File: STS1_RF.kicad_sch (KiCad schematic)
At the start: 79 parts, among them J1 UHF, Q1 SQ2318, Q3 SQ2318, Q4 SQ2318, U10 TQP3M9036, U11 NL17SV04XV5T2G, U16 F2972, U2 LP2985-1.8, U4 74LVC2G74, U5 TYKTBCSANF-26.000000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

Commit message: Fix mismatch between footprint and part number for C48, C72, C74, R13, R24, R21, R27, R28, R30, R31
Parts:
- R13, R21, R24: PartNumber CR0402-FX-3302GLF -> (none)
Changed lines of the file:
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@@
       (effects (font (size 1.27 1.27)) hide)
     )
-    (property "Description" "Resistor, 0402, 5%, 1/16W" (id 4) (at 157.48 166.37 0)
+    (property "Description" "" (id 4) (at 157.48 166.37 0)
       (effects (font (size 1.27 1.27)) hide)
     )
@@
       (effects (font (size 1.27 1.27)) hide)
     )
-    (property "PartNumber" "CR0402-FX-3302GLF" (id 6) (at 157.48 166.37 0)
+    (property "PartNumber" "" (id 6) (at 157.48 166.37 0)
       (effects (font (size 1.27 1.27)) hide)
     )
@@
       (effects (font (size 1.27 1.27)) hide)
     )
-    (property "Description" "Resistor, 0402, 5%, 1/16W" (id 4) (at 60.96 121.92 0)
+    (property "Description" "" (id 4) (at 60.96 121.92 0)
       (effects (font (size 1.27 1.27)) hide)
     )
@@
       (effects (font (size 1.27 1.27)) hide)
     )
-    (property "PartNumber" "CR0402-FX-3302GLF" (id 6) (at 60.96 121.92 0)
+    (property "PartNumber" "" (id 6) (at 60.96 121.92 0)
       (effects (font (size 1.27 1.27)) hide)
     )
@@
       (effects (font (size 1.27 1.27)) hide)
     )
-    (property "Description" "Resistor, 0402, 5%, 1/16W" (id 4) (at 72.39 121.92 0)
+    (property "Description" "" (id 4) (at 72.39 121.92 0)
       (effects (font (size 1.27 1.27)) hide)
     )
@@
       (effects (font (size 1.27 1.27)) hide)
     )
-    (property "PartNumber" "CR0402-FX-3302GLF" (id 6) (at 72.39 121.92 0)
-      (effects (font (size 1.27 1.27)) hide)
-    )
+    (property "PartNumber" "" (id 6) (at 72.39 121.92 0)
+      (effects (font (size 1.27 1.27)) hide)
+    )

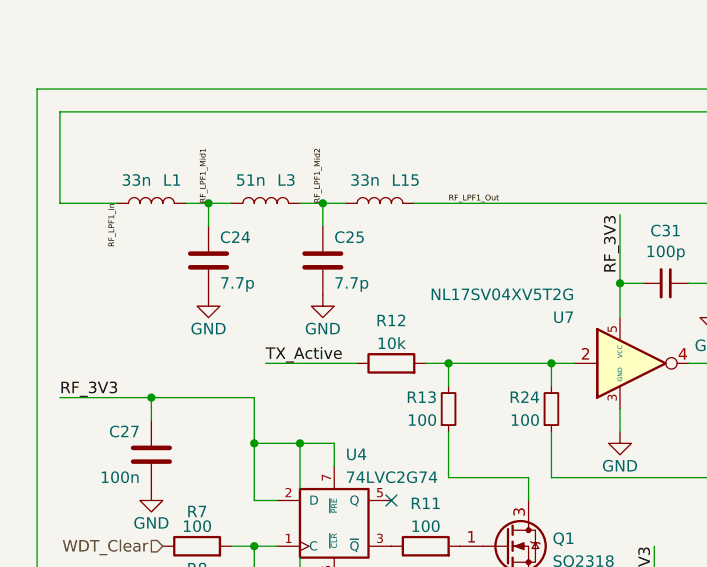
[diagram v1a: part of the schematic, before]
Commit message: Update values of components in the RF subsystem and swap CL instead of LC filter (L14 and C67)
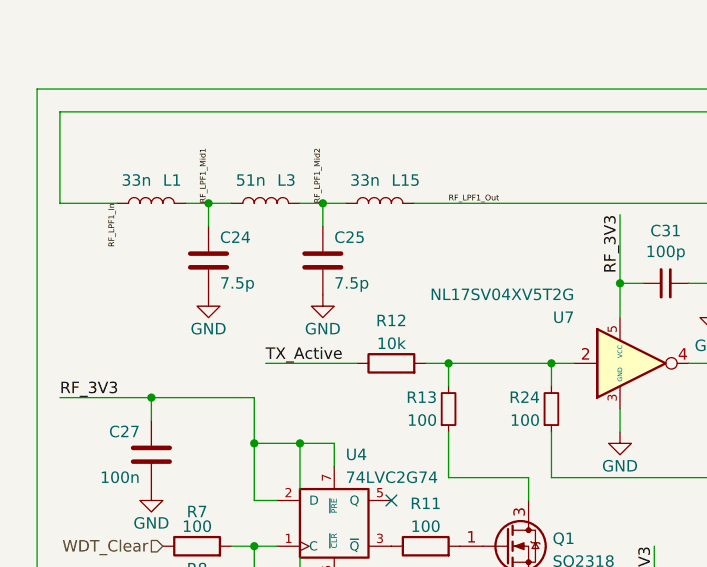
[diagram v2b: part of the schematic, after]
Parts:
- C24, C25: value 7.7p -> 7.5p
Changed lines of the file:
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@@
       (effects (font (size 1.27 1.27)) (justify left))
     )
-    (property "Value" "7.7p" (id 1) (at 48.26 107.95 0)
+    (property "Value" "7.5p" (id 1) (at 48.26 107.95 0)
       (effects (font (size 1.27 1.27)) (justify left))
     )
@@
       (effects (font (size 1.27 1.27)) (justify left))
     )
-    (property "Value" "7.7p" (id 1) (at 35.56 107.95 0)
-      (effects (font (size 1.27 1.27)) (justify left))
-    )
+    (property "Value" "7.5p" (id 1) (at 35.56 107.95 0)
+      (effects (font (size 1.27 1.27)) (justify left))
+    )

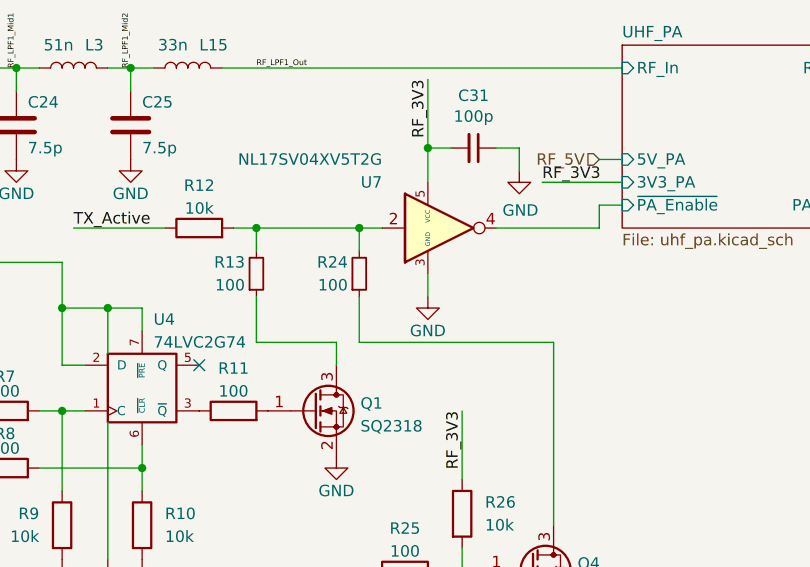
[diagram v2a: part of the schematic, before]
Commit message: Add latchup protection circuits
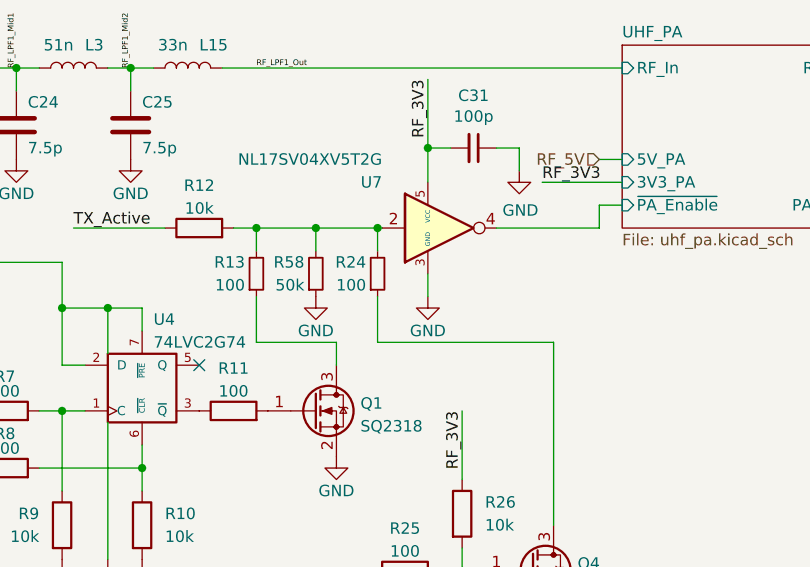
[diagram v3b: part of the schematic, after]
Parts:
- added R58: 50k, Resistor_SMD:R_0603_1608Metric, symbol Device:R_Small
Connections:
- net GND: now also R58.1
- net at R12.2, R13.2, R24.2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: now also R58.2
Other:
- moved on the sheet: R24
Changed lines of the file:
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@@
   (junction (at 158.75 73.66) (diameter 0) (color 0 0 0 0)
   )
+  (junction (at 74.422 116.84) (diameter 0) (color 0 0 0 0)
+  )
   (junction (at 66.04 66.04) (diameter 0) (color 0 0 0 0)
   )
@@
   (junction (at 181.61 147.32) (diameter 0) (color 0 0 0 0)
   )
-  (junction (at 72.39 116.84) (diameter 0) (color 0 0 0 0)
-  )
   (junction (at 248.92 101.6) (diameter 0) (color 0 0 0 0)
   )
@@
   )
   (junction (at 152.4 50.8) (diameter 0) (color 0 0 0 0)
+  )
+  (junction (at 67.564 116.84) (diameter 0) (color 0 0 0 0)
   )
   (junction (at 48.26 143.51) (diameter 0) (color 0 0 0 0)
@@
     (stroke (width 0) (type default) (color 0 0 0 0))
   )
+  (wire (pts (xy 67.564 116.84) (xy 74.422 116.84))
+    (stroke (width 0) (type default) (color 0 0 0 0))
+  )
   (wire (pts (xy 100.33 55.88) (xy 120.65 55.88))
     (stroke (width 0) (type default) (color 0 0 0 0))
@@
     (stroke (width 0) (type default) (color 0 0 0 0))
   )
-  (wire (pts (xy 72.39 129.54) (xy 93.98 129.54))
-    (stroke (width 0) (type default) (color 0 0 0 0))
-  )
   (wire (pts (xy 48.26 55.88) (xy 48.26 66.04))
     (stroke (width 0) (type default) (color 0 0 0 0))
@@
     (stroke (width 0) (type default) (color 0 0 0 0))
   )
+  (wire (pts (xy 93.98 129.54) (xy 74.422 129.54))
+    (stroke (width 0) (type default) (color 0 0 0 0))
+  )
   (wire (pts (xy 149.86 153.67) (xy 152.4 153.67))
     (stroke (width 0) (type default) (color 0 0 0 0))
@@
     (stroke (width 0) (type default) (color 0 0 0 0))
   )
-  (wire (pts (xy 72.39 124.46) (xy 72.39 129.54))
-    (stroke (width 0) (type default) (color 0 0 0 0))
-  )
   (wire (pts (xy 152.4 99.06) (xy 170.18 99.06))
     (stroke (width 0) (type default) (color 0 0 0 0))
@@
     (stroke (width 0) (type default) (color 0 0 0 0))
   )
+  (wire (pts (xy 74.422 129.54) (xy 74.422 124.46))
+    (stroke (width 0) (type default) (color 0 0 0 0))
+  )
   (wire (pts (xy 176.53 73.66) (xy 179.07 73.66))
     (stroke (width 0) (type default) (color 0 0 0 0))
   )
+  (wire (pts (xy 74.422 116.84) (xy 74.93 116.84))
+    (stroke (width 0) (type default) (color 0 0 0 0))
+  )
   (wire (pts (xy 87.63 116.84) (xy 99.06 116.84))
     (stroke (width 0) (type default) (color 0 0 0 0))
@@
     (stroke (width 0) (type default) (color 0 0 0 0))
   )
+  (wire (pts (xy 67.564 116.84) (xy 67.564 119.38))
+    (stroke (width 0) (type default) (color 0 0 0 0))
+  )
   (wire (pts (xy 165.1 21.59) (xy 172.72 21.59))
     (stroke (width 0) (type default) (color 0 0 0 0))
@@
     (stroke (width 0) (type default) (color 0 0 0 0))
   )
-  (wire (pts (xy 60.96 116.84) (xy 72.39 116.84))
+  (wire (pts (xy 60.96 116.84) (xy 67.564 116.84))
     (stroke (width 0) (type default) (color 0 0 0 0))
   )
@@
     (stroke (width 0) (type default) (color 0 0 0 0))
   )
-  (wire (pts (xy 72.39 116.84) (xy 74.93 116.84))
-    (stroke (width 0) (type default) (color 0 0 0 0))
-  )
   (wire (pts (xy 127 149.86) (xy 124.46 149.86))
     (stroke (width 0) (type default) (color 0 0 0 0))
@@
     (stroke (width 0) (type default) (color 0 0 0 0))
   )
-  (wire (pts (xy 72.39 116.84) (xy 72.39 119.38))
-    (stroke (width 0) (type default) (color 0 0 0 0))
-  )
   (wire (pts (xy 83.82 152.4) (xy 83.82 154.94))
     (stroke (width 0) (type default) (color 0 0 0 0))
@@
   )
   (wire (pts (xy 92.71 111.76) (xy 101.6 111.76))
+    (stroke (width 0) (type default) (color 0 0 0 0))
+  )
+  (wire (pts (xy 74.422 116.84) (xy 74.422 119.38))
     (stroke (width 0) (type default) (color 0 0 0 0))
   )
@@
     (pin "2")
   )
-  (symbol (lib_id "Device:R_Small") (at 72.39 121.92 0) (mirror x) (unit 1)
-    (in_bom yes) (on_board yes)
-    (property "Reference" "R24" (id 0) (at 71.12 120.65 0)
-      (effects (font (size 1.27 1.27)) (justify right))
-    )
-    (property "Value" "100" (id 1) (at 71.12 123.19 0)
-      (effects (font (size 1.27 1.27)) (justify right))
-    )
-    (property "Footprint" "Resistor_SMD:R_0603_1608Metric" (id 2) (at 72.39 121.92 0)
-      (effects (font (size 1.27 1.27)) hide)
-    )
-    (property "Datasheet" "~" (id 3) (at 72.39 121.92 0)
-      (effects (font (size 1.27 1.27)) hide)
-    )
-    (property "Description" "" (id 4) (at 72.39 121.92 0)
-      (effects (font (size 1.27 1.27)) hide)
-    )
-    (property "Mnf." "" (id 5) (at 72.39 121.92 0)
-      (effects (font (size 1.27 1.27)) hide)
-    )
-    (property "PartNumber" "" (id 6) (at 72.39 121.92 0)
+  (symbol (lib_id "Device:R_Small") (at 74.422 121.92 0) (mirror x) (unit 1)
+    (in_bom yes) (on_board yes)
+    (property "Reference" "R24" (id 0) (at 73.152 120.65 0)
+      (effects (font (size 1.27 1.27)) (justify right))
+    )
+    (property "Value" "100" (id 1) (at 73.152 123.19 0)
+      (effects (font (size 1.27 1.27)) (justify right))
+    )
+    (property "Footprint" "Resistor_SMD:R_0603_1608Metric" (id 2) (at 74.422 121.92 0)
+      (effects (font (size 1.27 1.27)) hide)
+    )
+    (property "Datasheet" "~" (id 3) (at 74.422 121.92 0)
+      (effects (font (size 1.27 1.27)) hide)
+    )
+    (property "Description" "" (id 4) (at 74.422 121.92 0)
+      (effects (font (size 1.27 1.27)) hide)
+    )
+    (property "Mnf." "" (id 5) (at 74.422 121.92 0)
+      (effects (font (size 1.27 1.27)) hide)
+    )
+    (property "PartNumber" "" (id 6) (at 74.422 121.92 0)
       (effects (font (size 1.27 1.27)) hide)
     )
@@
     )
     (pin "1")
+  )
+  (symbol (lib_id "Device:R_Small") (at 67.564 121.92 0) (mirror x) (unit 1)
+    (in_bom yes) (on_board yes)
+    (property "Reference" "R58" (id 0) (at 66.294 120.65 0)
+      (effects (font (size 1.27 1.27)) (justify right))
+    )
+    (property "Value" "50k" (id 1) (at 66.294 123.19 0)
+      (effects (font (size 1.27 1.27)) (justify right))
+    )
+    (property "Footprint" "Resistor_SMD:R_0603_1608Metric" (id 2) (at 67.564 121.92 0)
+      (effects (font (size 1.27 1.27)) hide)
+    )
+    (property "Datasheet" "~" (id 3) (at 67.564 121.92 0)
+      (effects (font (size 1.27 1.27)) hide)
+    )
+    (property "Description" "" (id 4) (at 67.564 121.92 0)
+      (effects (font (size 1.27 1.27)) hide)
+    )
+    (property "Mnf." "" (id 5) (at 67.564 121.92 0)
+      (effects (font (size 1.27 1.27)) hide)
+    )
+    (property "PartNumber" "" (id 6) (at 67.564 121.92 0)
+      (effects (font (size 1.27 1.27)) hide)
+    )
+    (pin "1")
+    (pin "2")
   )
   (symbol (lib_id "power:GND") (at 227.33 146.05 0) (unit 1)
@@
     (pin "2")
   )
+  (symbol (lib_id "power:GND") (at 67.564 124.46 0) (unit 1)
+    (in_bom yes) (on_board yes)
+    (property "Reference" "#PWR058" (id 0) (at 67.564 130.81 0)
+      (effects (font (size 1.27 1.27)) hide)
+    )
+    (property "Value" "GND" (id 1) (at 67.564 128.27 0))
+    (property "Footprint" "" (id 2) (at 67.564 124.46 0)
+      (effects (font (size 1.27 1.27)) hide)
+    )
+    (property "Datasheet" "" (id 3) (at 67.564 124.46 0)
+      (effects (font (size 1.27 1.27)) hide)
+    )
+    (pin "1")
+  )
   (symbol (lib_id "power:GND") (at 27.94 130.81 0) (unit 1)
